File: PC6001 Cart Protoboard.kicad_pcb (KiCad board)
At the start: 2 copper layers, 97.8 x 80.6 mm, 7 parts, among them J1 PC-6001 edge connector

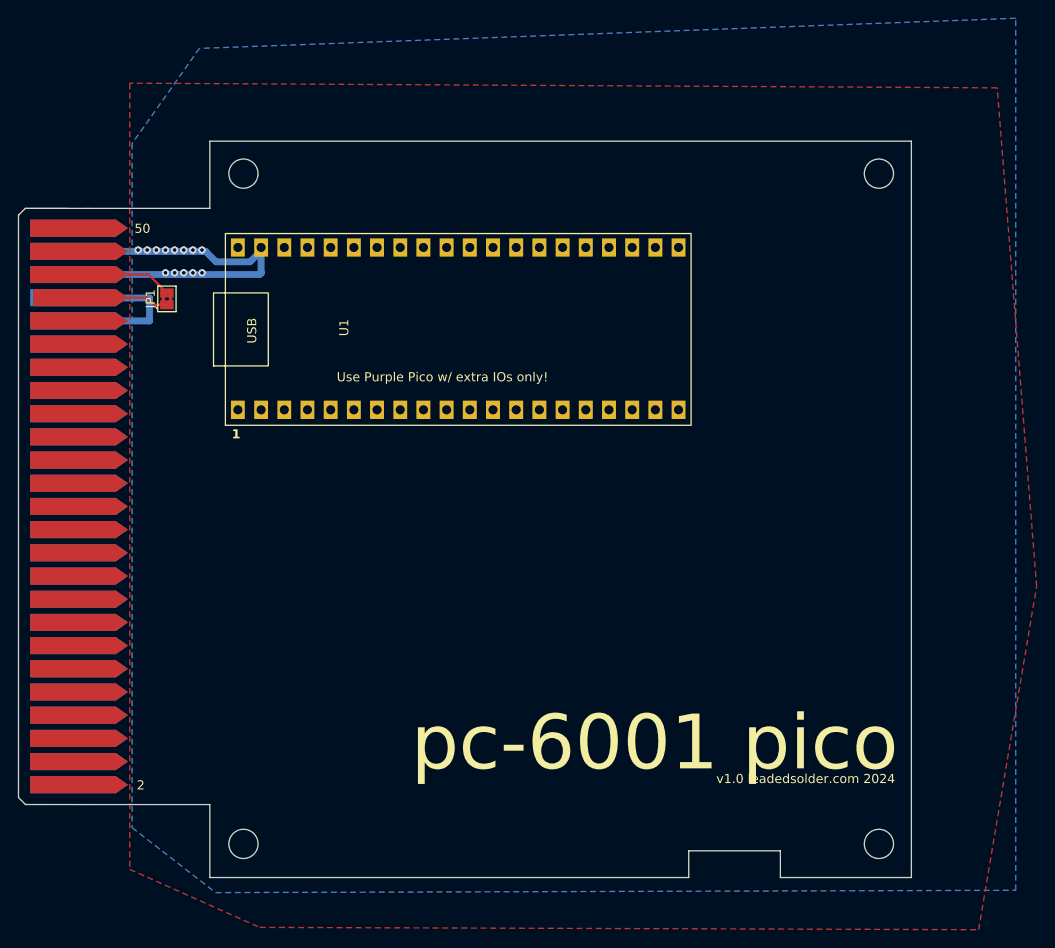
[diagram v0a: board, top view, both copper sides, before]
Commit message: ESP32 added to board
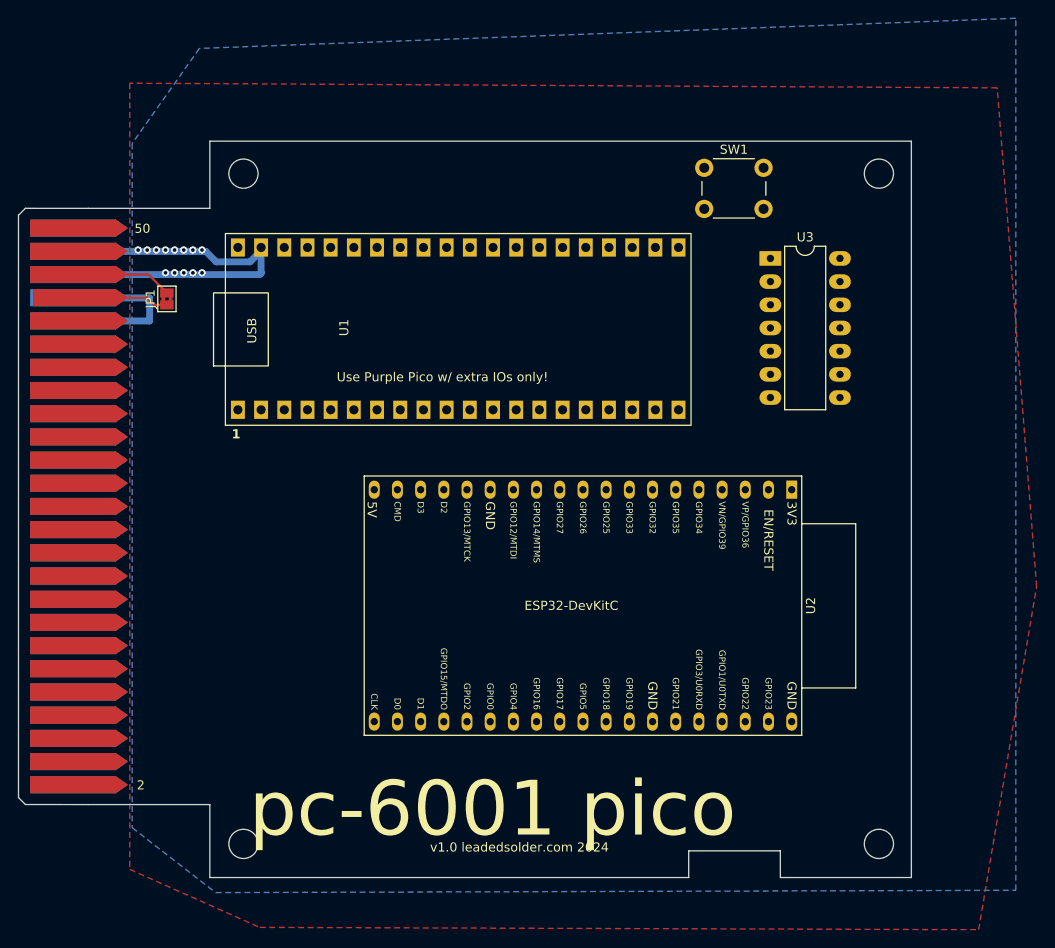
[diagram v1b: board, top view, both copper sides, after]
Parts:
- added SW1: PicoReset, Button_Switch_THT:SW_PUSH_6mm, F.Cu at (195.8, 71.5)
- added U2: ESP32-DevKitC, Espressif:ESP32-DevKitC, F.Cu at (205.3, 106.8)
- added U3: 74LS32, Package_DIP:DIP-14_W7.62mm_LongPads, F.Cu at (203.0, 81.4)
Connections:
- U1 pad 1: unconnected-(U1-GPIO_0-Pad1) -> /ESP_RX
- U1 pad 2: unconnected-(U1-GPIO_1-Pad2) -> /ESP_TX
- U1 pad 21: unconnected-(U1-GPIO_18-Pad21) -> /~{ROMSEL}
- U1 pad 31: unconnected-(U1-GPIO_27-Pad31) -> /ESP_CMD
- U1 pad 32: unconnected-(U1-GPIO_28-Pad32) -> /ESP_PROC
- U1 pad 33: unconnected-(U1-GPIO_29-Pad33) -> /ESP_INT

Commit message: Z80 data, addr bus
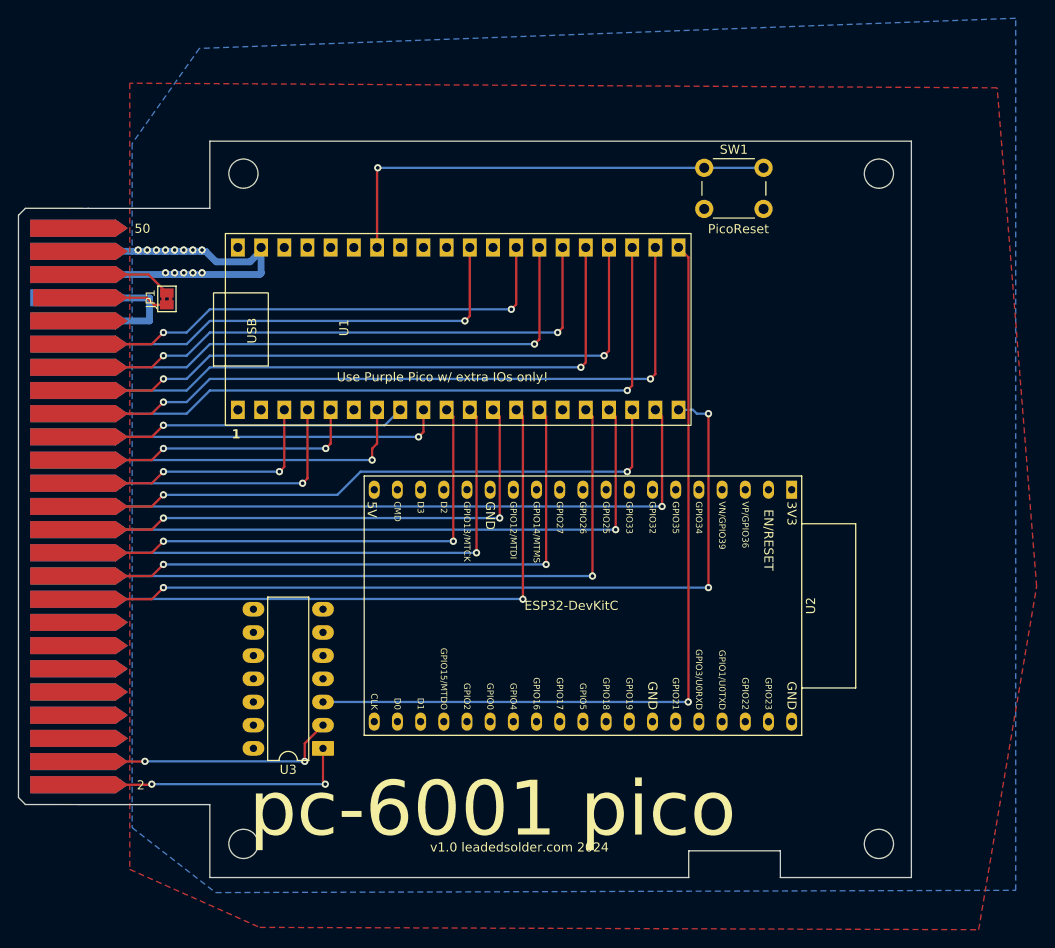
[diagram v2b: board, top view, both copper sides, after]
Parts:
- moved U3 72.7 mm to (154.0, 135.1), turned to 180 degrees
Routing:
- net /a15: track 0.00 -> 95.4 mm, vias 0 -> 3
- net /~{ROMSEL}: track 0.00 -> 90.2 mm, vias 0 -> 1
- net /d0: track 0.00 -> 82.2 mm, vias 0 -> 2
- net /d1: track 0.00 -> 80.4 mm, vias 0 -> 1
- net /a11: track 0.00 -> 78.2 mm, vias 0 -> 1
- net /a14: track 0.00 -> 78.2 mm, vias 0 -> 1
- net /a12: track 0.00 -> 75.7 mm, vias 0 -> 1
- net /d2: track 0.00 -> 74.6 mm, vias 0 -> 2
- net /a9: track 0.00 -> 73.1 mm, vias 0 -> 1
- net /d3: track 0.00 -> 72.8 mm, vias 0 -> 1
- net /a10: track 0.00 -> 72.4 mm, vias 0 -> 2
- net /a13: track 0.00 -> 72.1 mm, vias 0 -> 2
- net /d4: track 0.00 -> 67.0 mm, vias 0 -> 2
- net /d5: track 0.00 -> 65.2 mm, vias 0 -> 1
- net /a7: track 0.00 -> 63.0 mm, vias 0 -> 1
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
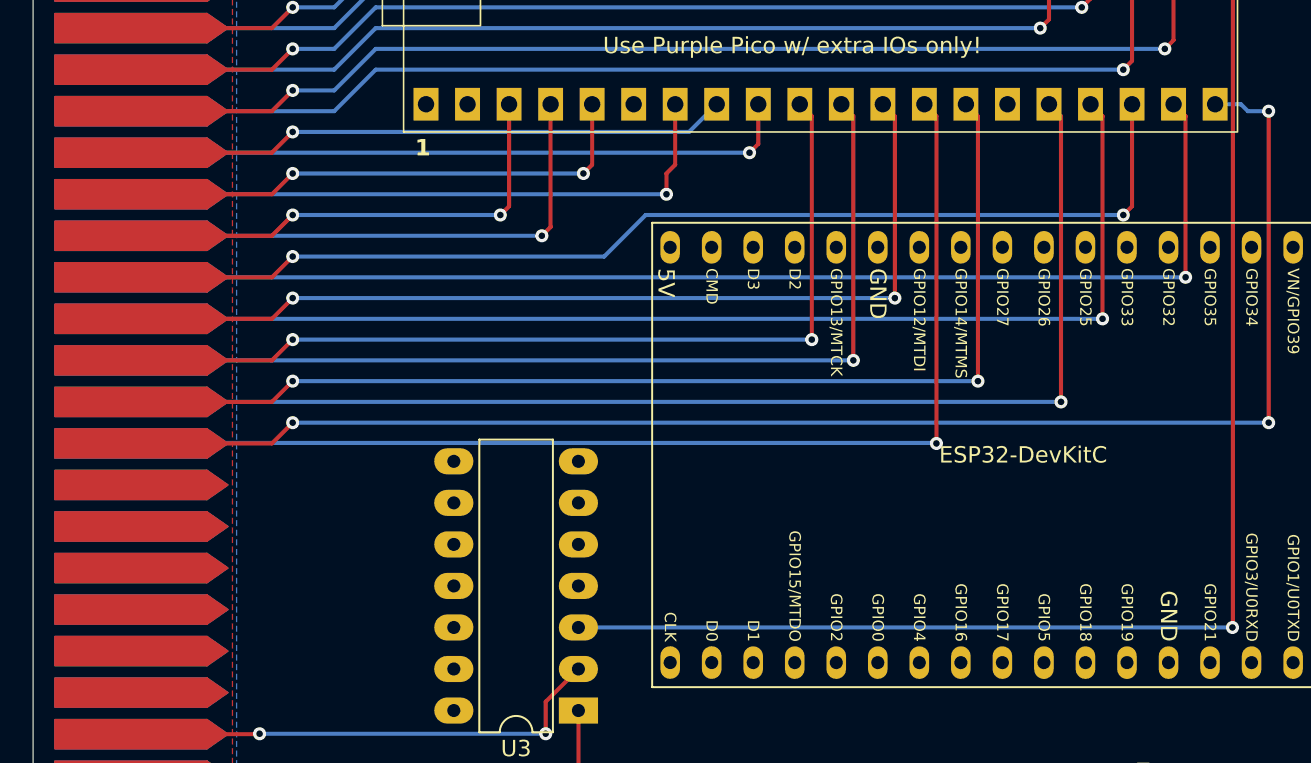
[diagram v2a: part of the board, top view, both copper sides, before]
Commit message: ESP32 connected
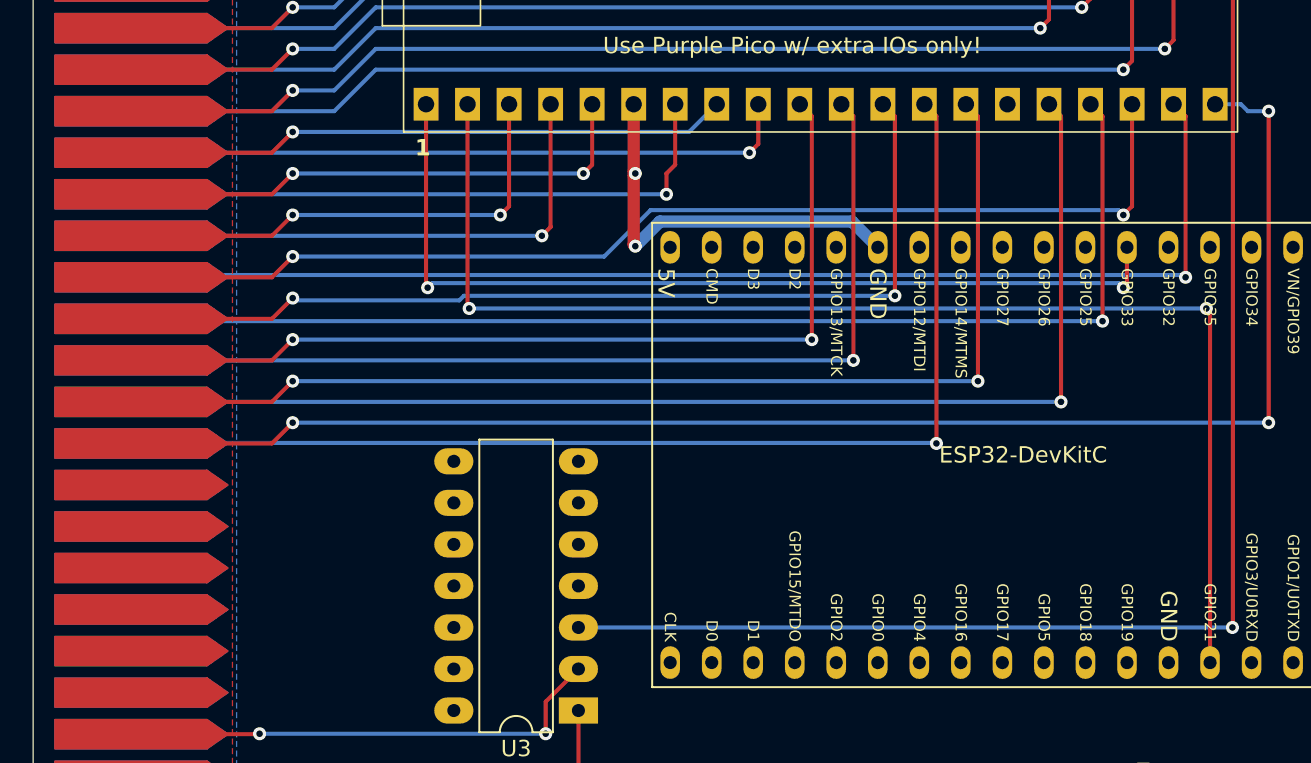
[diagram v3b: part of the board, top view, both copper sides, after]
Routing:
- net /ESP_TX: track 0.00 -> 79.4 mm, vias 0 -> 2
- net /ESP_RX: track 0.00 -> 56.6 mm, vias 0 -> 2
- net GND: track 24.9 -> 49.8 mm, vias 0 -> 2

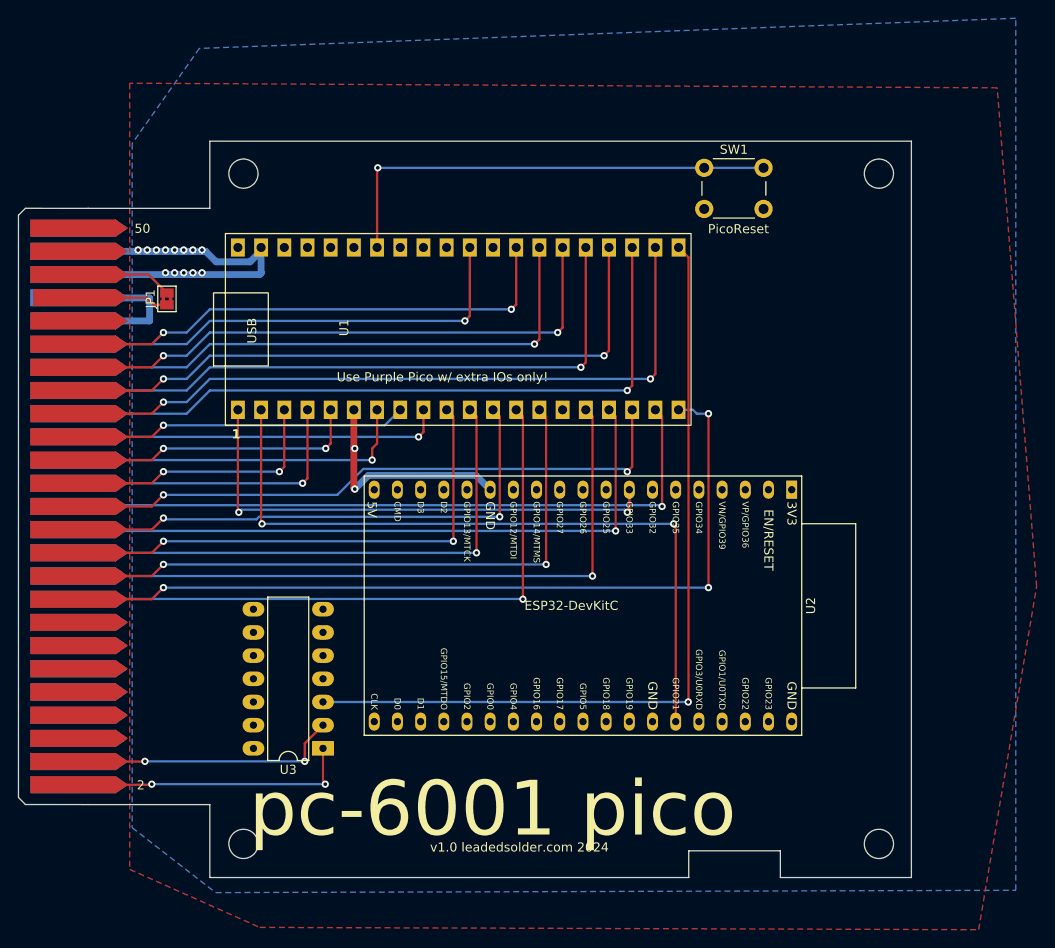
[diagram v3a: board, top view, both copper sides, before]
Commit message: ESP-reset button
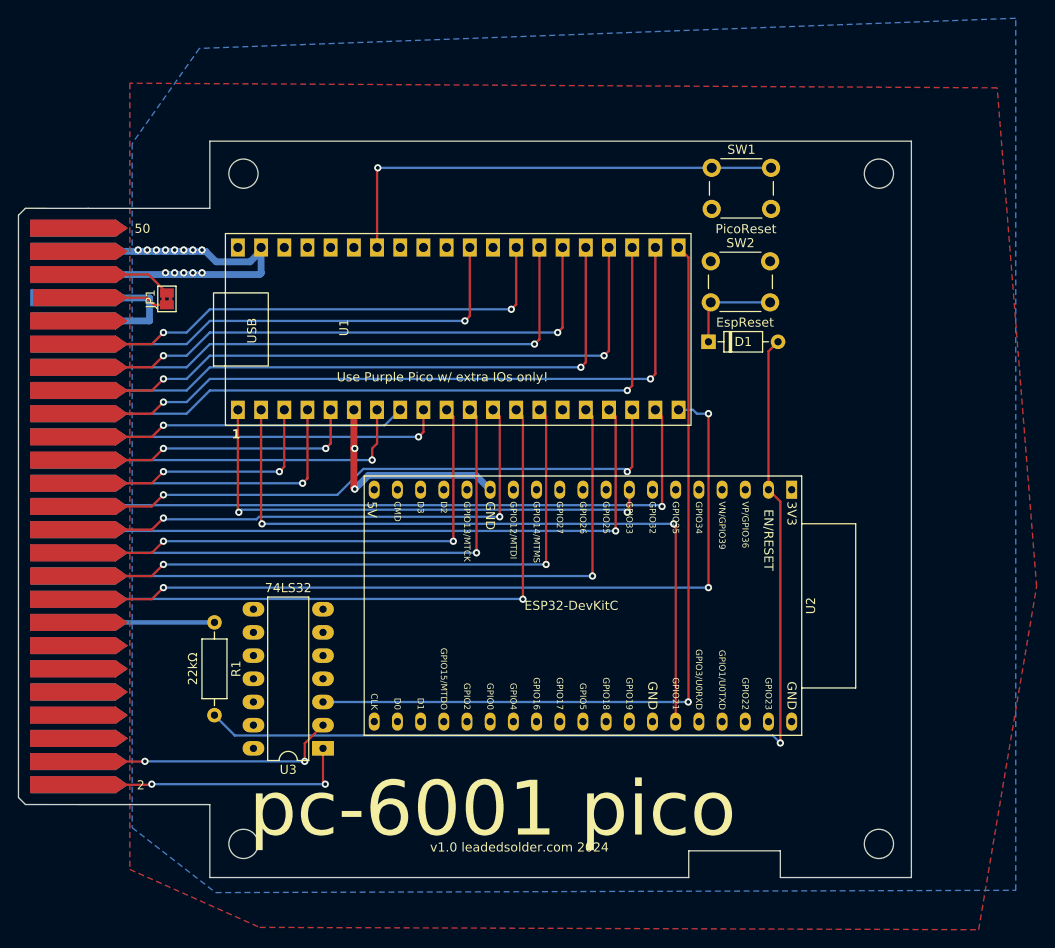
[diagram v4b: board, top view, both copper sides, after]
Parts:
- added D1: D, Diode_THT:D_DO-35_SOD27_P7.62mm_Horizontal, F.Cu at (196.2, 90.6)
- added R1: 22kΩ, Resistor_THT:R_Axial_DIN0207_L6.3mm_D2.5mm_P10.16mm_Horizontal, F.Cu at (142.1, 121.3)
- added SW2: EspReset, Button_Switch_THT:SW_PUSH_6mm, F.Cu at (196.5, 81.7)
- moved SW1 0.82 mm to (196.6, 71.5)
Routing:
- net /ESP_RST: track 0.00 -> 108.2 mm, vias 0 -> 1
- net /RESET: track 0.00 -> 18.3 mm
- net Net-(D1-K): track 0.00 -> 10.9 mm

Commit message: Stub out ram select
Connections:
- U3 pad 4: (no net) -> /~{EXCAS}
- U3 pad 5: (no net) -> /~{RAS}
- U3 pad 6: (no net) -> /~{RAMSEL}
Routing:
- net /~{RAS}: track 0.00 -> 46.0 mm, vias 0 -> 2
- net /~{EXCAS}: track 0.00 -> 31.9 mm, vias 0 -> 1
- net GND: track 49.8 -> 54.0 mm, vias 2 -> 3
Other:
- board text added: "~{RAMSEL}"
- board text added: "~{ROMSEL}"
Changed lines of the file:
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@@
 	(net 90 "+3.3V")
 	(net 91 "Net-(D1-K)")
+	(net 92 "/~{RAMSEL}")
 	(footprint "PC6001 Edge Connector:PC6001 Cartridge Connector"
 		(layer "F.Cu")
@@
 			(layers "*.Cu" "*.Mask")
 			(remove_unused_layers no)
+			(net 13 "/~{EXCAS}")
+			(pintype "input")
 		)
 		(pad "5" thru_hole oval
@@
 			(layers "*.Cu" "*.Mask")
 			(remove_unused_layers no)
+			(net 3 "/~{RAS}")
+			(pintype "input")
 		)
 		(pad "6" thru_hole oval
@@
 			(layers "*.Cu" "*.Mask")
 			(remove_unused_layers no)
+			(net 92 "/~{RAMSEL}")
+			(pintype "output")
 		)
 		(pad "7" thru_hole oval
@@
 		(layer "Edge.Cuts")
 	)
+	(gr_text "~{RAMSEL}"
+		(at 161.671 123.063 0)
+		(layer "B.SilkS")
+		(effects
+			(font
+				(size 1 1)
+				(thickness 0.15)
+			)
+			(justify left bottom mirror)
+		)
+	)
 	(gr_text "1"
 		(at 134.62 139.7 0)
@@
 		)
 	)
+	(gr_text "~{ROMSEL}"
+		(at 161.925 130.683 0)
+		(layer "B.SilkS")
+		(effects
+			(font
+				(size 1 1)
+				(thickness 0.15)
+			)
+			(justify left bottom mirror)
+		)
+	)
 	(gr_text "50"
 		(at 133.35 78.74 0)
@@
 	)
 	(segment
+		(start 149.479 140.335)
+		(end 149.479 125.095)
+		(width 0.25)
+		(layer "F.Cu")
+		(net 3)
+	)
+	(via
+		(at 149.479 125.095)
+		(size 0.8)
+		(drill 0.4)
+		(layers "F.Cu" "B.Cu")
+		(net 3)
+	)
+	(via
+		(at 149.479 140.335)
+		(size 0.8)
+		(drill 0.4)
+		(layers "F.Cu" "B.Cu")
+		(net 3)
+	)
+	(segment
+		(start 149.479 125.095)
+		(end 149.654 124.92)
+		(width 0.25)
+		(layer "B.Cu")
+		(net 3)
+	)
+	(segment
+		(start 123.825 139.065)
+		(end 133.985 139.065)
+		(width 0.25)
+		(layer "B.Cu")
+		(net 3)
+	)
+	(segment
+		(start 135.255 140.335)
+		(end 149.479 140.335)
+		(width 0.25)
+		(layer "B.Cu")
+		(net 3)
+	)
+	(segment
+		(start 149.654 124.92)
+		(end 154 124.92)
+		(width 0.25)
+		(layer "B.Cu")
+		(net 3)
+	)
+	(segment
+		(start 133.985 139.065)
+		(end 135.255 140.335)
+		(width 0.25)
+		(layer "B.Cu")
+		(net 3)
+	)
+	(segment
 		(start 142.113 121.285)
 		(end 123.825 121.285)
@@
 	)
 	(segment
+		(start 133.477 128.905)
+		(end 136.271 126.111)
+		(width 0.25)
+		(layer "F.Cu")
+		(net 13)
+	)
+	(segment
+		(start 123.825 128.905)
+		(end 133.477 128.905)
+		(width 0.25)
+		(layer "F.Cu")
+		(net 13)
+	)
+	(via
+		(at 136.271 126.111)
+		(size 0.8)
+		(drill 0.4)
+		(layers "F.Cu" "B.Cu")
+		(net 13)
+	)
+	(segment
+		(start 152.651 126.111)
+		(end 154 127.46)
+		(width 0.25)
+		(layer "B.Cu")
+		(net 13)
+	)
+	(segment
+		(start 136.271 126.111)
+		(end 152.651 126.111)
+		(width 0.25)
+		(layer "B.Cu")
+		(net 13)
+	)
+	(segment
 		(start 134.889 83.185)
 		(end 136.906 85.202)
@@
 	)
 	(segment
+		(start 190.09 132.15)
+		(end 190.09 127.918)
+		(width 0.25)
+		(layer "F.Cu")
+		(net 19)
+	)
+	(segment
 		(start 157.38 102.335)
 		(end 157.38 106.58)
@@
 		(net 19)
 	)
+	(segment
+		(start 190.09 127.918)
+		(end 190.119 127.889)
+		(width 0.25)
+		(layer "F.Cu")
+		(net 19)
+	)
 	(via
 		(at 157.48 102.235)
 		(size 0.8)
 		(drill 0.4)
+		(layers "F.Cu" "B.Cu")
+		(net 19)
+	)
+	(via
+		(at 190.119 127.889)
+		(size 0.8)
+		(drill 0.4)
